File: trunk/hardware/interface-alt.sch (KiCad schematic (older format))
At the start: 19 parts, among them SW1 DIPSW4_DIP, U4 GTL2003

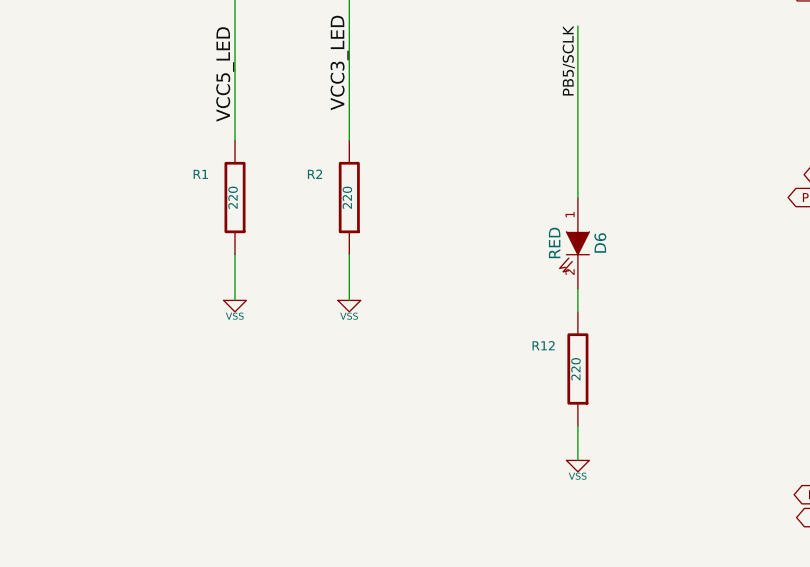
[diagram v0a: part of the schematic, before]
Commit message: Changed all 220ohm LED resistors to 1Kohm. This is how I actually built the first r116 test board. The LEDs are still too bright for my liking, actually. This way, we may also save a little battery power.
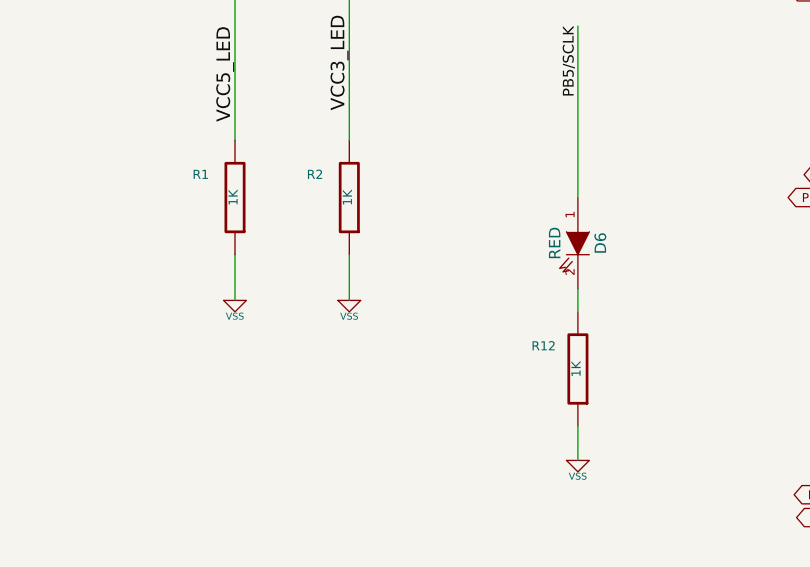
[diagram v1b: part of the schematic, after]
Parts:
- R1, R12, R2: value 220 -> 1K
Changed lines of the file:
@@
 Sheet 6 6
 Title "FREAKDUINO-CHIBI 2.4GHz"
-Date "12 aug 2013"
+Date "13 aug 2013"
 Rev "v1.1"
 Comp "KiCAD version by Gruvin"
@@
 P 6450 5300
 F 0 "R1" H 6600 5200 40  0000 C CNN
-F 1 "220" V 6457 5301 40  0000 C CNN
+F 1 "1K" V 6457 5301 40  0000 C CNN
 F 2 "" V 6380 5300 30  0000 C CNN
 F 3 "" H 6450 5300 30  0000 C CNN
@@
 P 6950 5300
 F 0 "R2" H 7100 5200 40  0000 C CNN
-F 1 "220" V 6957 5301 40  0000 C CNN
+F 1 "1K" V 6957 5301 40  0000 C CNN
 F 2 "" V 6880 5300 30  0000 C CNN
 F 3 "" H 6950 5300 30  0000 C CNN
@@
 P 7950 6050
 F 0 "R12" H 8100 5950 40  0000 C CNN
-F 1 "220" V 7957 6051 40  0000 C CNN
+F 1 "1K" V 7957 6051 40  0000 C CNN
 F 2 "" V 7880 6050 30  0000 C CNN
 F 3 "" H 7950 6050 30  0000 C CNN

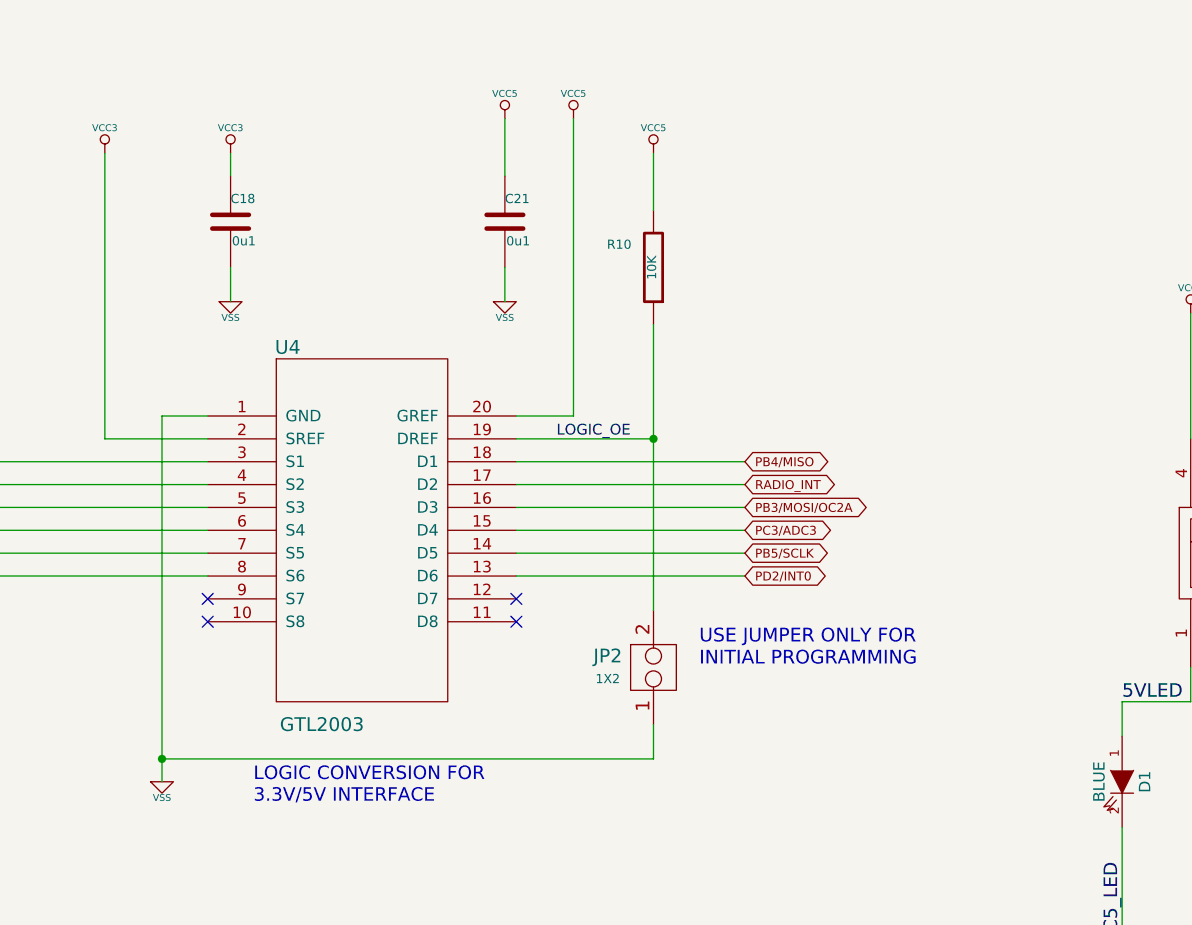
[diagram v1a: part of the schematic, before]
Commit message: Numberous more problems with the circuit design and PCB layout errors found and corrected as a result of debugging and making the RF section work, today, finally.
There remains and issue with the SPI port disable jumper not working as it should -- I think.  I got around this by fluke, when I realised that holding down the reset button (somehow) enables my AVR ISP mkII to program the AVR chip, despite the suspected SPI bus conflict between the ISP and level shofter chip. (Not that any of that makes sense to me right now. But that's what seemed to be the case, at the time. I'll sort it later.)
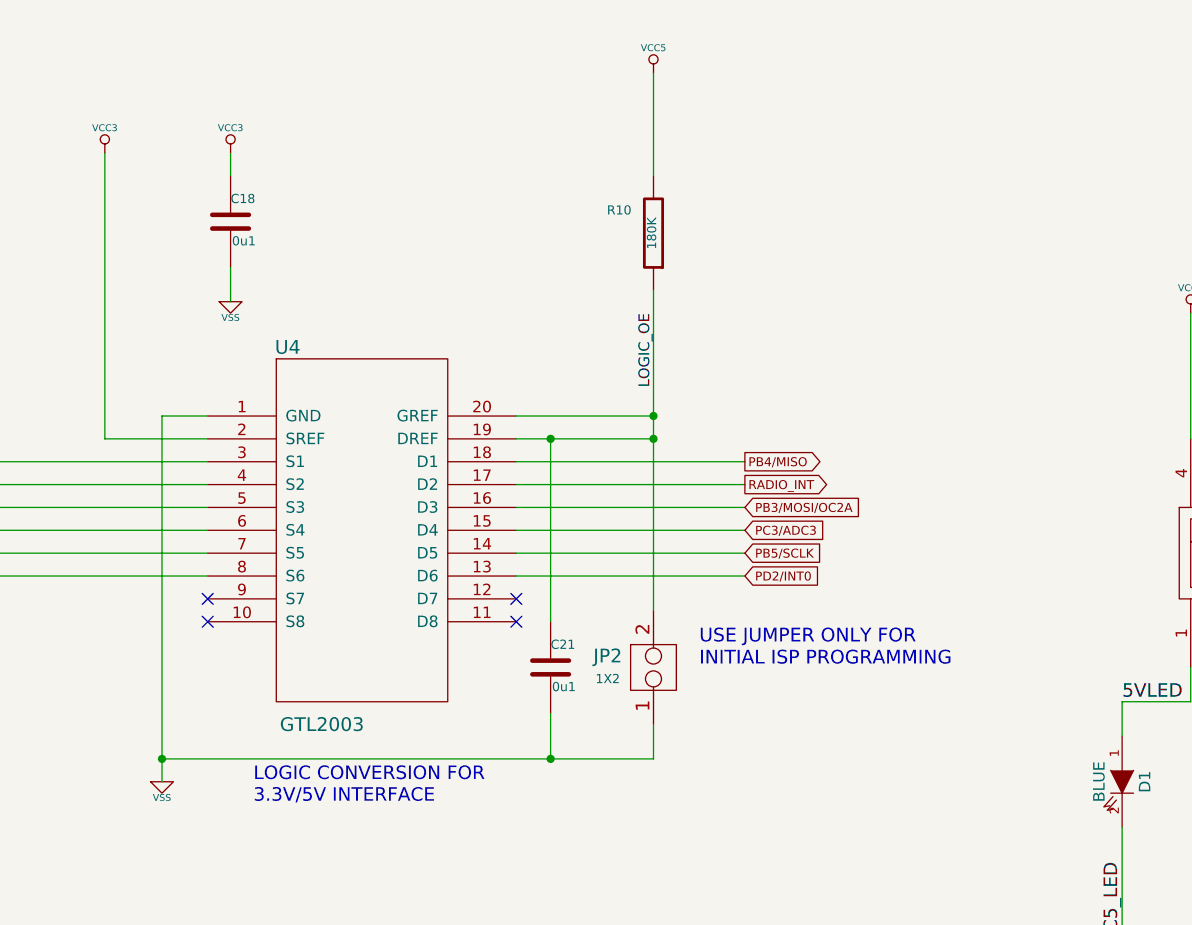
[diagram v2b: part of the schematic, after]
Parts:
- R10: value 10K -> 180K
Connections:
- net LOGIC_OE: now also C21.1, U4.20 (GREF)
- net VCC5: no longer C21.1, U4.20 (GREF)
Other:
- note added: "USE JUMPER ONLY FOR\nINITIAL ISP PROGRAMMING"
- note removed: "USE JUMPER ONLY FOR\nINITIAL PROGRAMMING"
- moved on the sheet: C21, R10
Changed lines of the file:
@@
 Sheet 6 6
 Title "FREAKDUINO-CHIBI 2.4GHz"
-Date "13 aug 2013"
+Date "16 aug 2013"
 Rev "v1.1"
 Comp "KiCAD version by Gruvin"
@@
 L R R10
 U 1 1 51E3DBD0
-P 4400 1950
-F 0 "R10" H 4550 1850 40  0000 C CNN
-F 1 "10K" V 4407 1951 40  0000 C CNN
-F 2 "" V 4330 1950 30  0000 C CNN
-F 3 "" H 4400 1950 30  0000 C CNN
-	1    4400 1950
+P 4400 1800
+F 0 "R10" H 4550 1700 40  0000 C CNN
+F 1 "180K" V 4407 1801 40  0000 C CNN
+F 2 "" V 4330 1800 30  0000 C CNN
+F 3 "" H 4400 1800 30  0000 C CNN
+	1    4400 1800
 	-1   0    0    1
 $EndComp
@@
 L C C21
 U 1 1 51E3DBD6
-P 3750 1750
-F 0 "C21" H 3750 1850 40  0000 L CNN
-F 1 "0u1" H 3756 1665 40  0000 L CNN
-F 2 "" H 3788 1600 30  0000 C CNN
-F 3 "" H 3750 1750 60  0000 C CNN
-	1    3750 1750
-	1    0    0    -1
-$EndComp
-$Comp
-L VSS #PWR051
-U 1 1 51E3DBDC
-P 3750 2100
-F 0 "#PWR051" H 3750 2100 30  0001 C CNN
-F 1 "VSS" H 3750 2030 30  0000 C CNN
-F 2 "" H 3750 2100 60  0000 C CNN
-F 3 "" H 3750 2100 60  0000 C CNN
-	1    3750 2100
-	1    0    0    -1
-$EndComp
-Wire Wire Line
-	3750 1300 3750 1550
-Wire Wire Line
-	3750 1950 3750 2100
+P 3950 3700
+F 0 "C21" H 3950 3800 40  0000 L CNN
+F 1 "0u1" H 3956 3615 40  0000 L CNN
+F 2 "" H 3988 3550 30  0000 C CNN
+F 3 "" H 3950 3700 60  0000 C CNN
+	1    3950 3700
+	1    0    0    -1
+$EndComp
 NoConn ~ 2450 3500
 NoConn ~ 2450 3400
@@
 NoConn ~ 3800 3400
 Wire Wire Line
-	4400 2200 4400 3450
-$Comp
-L VSS #PWR052
+	4400 2050 4400 3450
+$Comp
+L VSS #PWR050
 U 1 1 51E3DBEA
 P 2250 4200
-F 0 "#PWR052" H 2250 4200 30  0001 C CNN
+F 0 "#PWR050" H 2250 4200 30  0001 C CNN
 F 1 "VSS" H 2250 4130 30  0000 C CNN
 F 2 "" H 2250 4200 60  0000 C CNN
@@
 Wire Wire Line
 	2450 3300 1300 3300
-Text Label 4300 2700 2    47   ~ 0
+Text Label 4400 2150 3    47   ~ 0
 LOGIC_OE
 Text GLabel 1300 2800 0    47   Input ~ 0
@@
 SLP_TR
 Wire Wire Line
-	4050 1300 4050 2600
-Wire Wire Line
 	2000 1450 2000 2700
 $Comp
@@
 $EndComp
 $Comp
-L VSS #PWR053
+L VSS #PWR051
 U 1 1 51E3DC0E
 P 2550 2100
-F 0 "#PWR053" H 2550 2100 30  0001 C CNN
+F 0 "#PWR051" H 2550 2100 30  0001 C CNN
 F 1 "VSS" H 2550 2030 30  0000 C CNN
 F 2 "" H 2550 2100 60  0000 C CNN
@@
 	2550 1950 2550 2100
 Wire Wire Line
-	4400 1450 4400 1700
+	4400 1100 4400 1550
 Text Notes 2650 4300 0    59   ~ 0
 LOGIC CONVERSION FOR\n3.3V/5V INTERFACE
@@
 	3800 3300 4800 3300
 $Comp
-L VCC5 #PWR054
-U 1 1 51E3DC24
-P 3750 1300
-F 0 "#PWR054" H 3750 1440 20  0001 C CNN
-F 1 "VCC5" H 3750 1410 30  0000 C CNN
-F 2 "" H 3750 1300 60  0000 C CNN
-F 3 "" H 3750 1300 60  0000 C CNN
-	1    3750 1300
-	1    0    0    -1
-$EndComp
-$Comp
-L VCC5 #PWR055
-U 1 1 51E3DC2A
-P 4050 1300
-F 0 "#PWR055" H 4050 1440 20  0001 C CNN
-F 1 "VCC5" H 4050 1410 30  0000 C CNN
-F 2 "" H 4050 1300 60  0000 C CNN
-F 3 "" H 4050 1300 60  0000 C CNN
-	1    4050 1300
-	1    0    0    -1
-$EndComp
-$Comp
-L VCC3 #PWR056
+L VCC3 #PWR052
 U 1 1 51E3DC30
 P 2000 1450
-F 0 "#PWR056" H 2000 1590 20  0001 C CNN
+F 0 "#PWR052" H 2000 1590 20  0001 C CNN
 F 1 "VCC3" H 2000 1560 30  0000 C CNN
 F 2 "" H 2000 1450 60  0000 C CNN
@@
 $EndComp
 $Comp
-L VCC3 #PWR057
+L VCC3 #PWR053
 U 1 1 51E3DC36
 P 2550 1450
-F 0 "#PWR057" H 2550 1590 20  0001 C CNN
+F 0 "#PWR053" H 2550 1590 20  0001 C CNN
 F 1 "VCC3" H 2550 1560 30  0000 C CNN
 F 2 "" H 2550 1450 60  0000 C CNN
@@
 $EndComp
 Text Notes 4600 3700 0    60   ~ 0
-USE JUMPER ONLY FOR\nINITIAL PROGRAMMING
+USE JUMPER ONLY FOR\nINITIAL ISP PROGRAMMING
 $Comp
 L DIPSW4_DIP SW1
@@
 	6450 4400 6450 5050
 $Comp
-L VSS #PWR058
+L VSS #PWR054
 U 1 1 51E3E179
 P 6450 5750
-F 0 "#PWR058" H 6450 5750 30  0001 C CNN
+F 0 "#PWR054" H 6450 5750 30  0001 C CNN
 F 1 "VSS" H 6450 5680 30  0000 C CNN
 F 2 "" H 6450 5750 60  0000 C CNN
@@
 $EndComp
 $Comp
-L VSS #PWR059
+L VSS #PWR055
 U 1 1 51E3E17F
 P 6950 5750
-F 0 "#PWR059" H 6950 5750 30  0001 C CNN
+F 0 "#PWR055" H 6950 5750 30  0001 C CNN
 F 1 "VSS" H 6950 5680 30  0000 C CNN
 F 2 "" H 6950 5750 60  0000 C CNN
@@
 VCC3_LED
 $Comp
-L VCC3 #PWR060
+L VCC3 #PWR056
 U 1 1 51E3E18C
 P 6950 2350
-F 0 "#PWR060" H 6950 2490 20  0001 C CNN
+F 0 "#PWR056" H 6950 2490 20  0001 C CNN
 F 1 "VCC3" H 6950 2460 30  0000 C CNN
 F 2 "" H 6950 2350 60  0000 C CNN
@@
 $EndComp
 $Comp
-L VCC5 #PWR061
+L VCC5 #PWR057
 U 1 1 51E3E192
 P 6750 2150
-F 0 "#PWR061" H 6750 2290 20  0001 C CNN
+F 0 "#PWR057" H 6750 2290 20  0001 C CNN
 F 1 "VCC5" H 6750 2260 30  0000 C CNN
 F 2 "" H 6750 2150 60  0000 C CNN
@@
 	4200 6300 4200 6600
 $Comp
-L VSS #PWR062
+L VSS #PWR058
 U 1 1 51E3E429
 P 4200 6600
-F 0 "#PWR062" H 4200 6600 30  0001 C CNN
+F 0 "#PWR058" H 4200 6600 30  0001 C CNN
 F 1 "VSS" H 4200 6530 30  0000 C CNN
 F 2 "" H 4200 6600 60  0000 C CNN
@@
 ISP CONNECTOR
 $Comp
-L VCC5 #PWR063
+L VCC5 #PWR059
 U 1 1 51E3E434
 P 4200 5750
-F 0 "#PWR063" H 4200 5890 20  0001 C CNN
+F 0 "#PWR059" H 4200 5890 20  0001 C CNN
 F 1 "VCC5" H 4200 5860 30  0000 C CNN
 F 2 "" H 4200 5750 60  0000 C CNN
@@
 $EndComp
 $Comp
-L VSS #PWR064
+L VSS #PWR060
 U 1 1 51E3E736
 P 7950 6450
-F 0 "#PWR064" H 7950 6450 30  0001 C CNN
+F 0 "#PWR060" H 7950 6450 30  0001 C CNN
 F 1 "VSS" H 7950 6380 30  0000 C CNN
 F 2 "" H 7950 6450 60  0000 C CNN
@@
 	9650 5600 9650 5850
 $Comp
-L VSS #PWR065
+L VSS #PWR061
 U 1 1 51E3E76E
 P 9650 5850
-F 0 "#PWR065" H 9650 5850 30  0001 C CNN
+F 0 "#PWR061" H 9650 5850 30  0001 C CNN
 F 1 "VSS" H 9650 5780 30  0000 C CNN
 F 2 "" H 9650 5850 60  0000 C CNN
@@
 	9100 2100 9100 1000
 $Comp
-L VSS #PWR066
+L VSS #PWR062
 U 1 1 51E3E798
 P 9650 2300
-F 0 "#PWR066" H 9650 2300 30  0001 C CNN
+F 0 "#PWR062" H 9650 2300 30  0001 C CNN
 F 1 "VSS" H 9650 2230 30  0000 C CNN
 F 2 "" H 9650 2300 60  0000 C CNN
@@
 Connection ~ 9650 2000
 $Comp
-L VCC5 #PWR067
+L VCC5 #PWR063
 U 1 1 51E3E7A3
 P 9400 1100
-F 0 "#PWR067" H 9400 1240 20  0001 C CNN
+F 0 "#PWR063" H 9400 1240 20  0001 C CNN
 F 1 "VCC5" H 9400 1210 30  0000 C CNN
 F 2 "" H 9400 1100 60  0000 C CNN
@@
 $EndComp
 $Comp
-L VCC3 #PWR068
+L VCC3 #PWR064
 U 1 1 51E3E7A9
 P 9650 1200
-F 0 "#PWR068" H 9650 1340 20  0001 C CNN
+F 0 "#PWR064" H 9650 1340 20  0001 C CNN
 F 1 "VCC3" H 9650 1310 30  0000 C CNN
 F 2 "" H 9650 1200 60  0000 C CNN
@@
 $EndComp
 $Comp
-L VCC_IN #PWR069
+L VCC_IN #PWR065
 U 1 1 51E3E7C7
 P 9100 1000
-F 0 "#PWR069" H 9100 1140 20  0001 C CNN
+F 0 "#PWR065" H 9100 1140 20  0001 C CNN
 F 1 "VCC_IN" H 9100 1110 30  0000 C CNN
 F 2 "" H 9100 1000 60  0000 C CNN
@@
 Text GLabel 9400 6700 0    39   BiDi ~ 0
 PC5/ADC5/SCL
-Text GLabel 4800 3000 2    39   BiDi ~ 0
+Text GLabel 4800 3000 2    39   Input ~ 0
 PB3/MOSI/OC2A
-Text GLabel 4800 2800 2    39   BiDi ~ 0
+Text GLabel 4800 2800 2    39   Output ~ 0
 PB4/MISO
-Text GLabel 4800 3200 2    39   BiDi ~ 0
+Text GLabel 4800 3200 2    39   Input ~ 0
 PB5/SCLK
-Text GLabel 4800 3300 2    39   BiDi ~ 0
+Text GLabel 4800 3300 2    39   Input ~ 0
 PD2/INT0
-Text GLabel 4800 3100 2    39   BiDi ~ 0
+Text GLabel 4800 3100 2    39   Input ~ 0
 PC3/ADC3
-Text GLabel 4800 2900 2    39   BiDi ~ 0
+Text GLabel 4800 2900 2    39   Output ~ 0
 RADIO_INT
 $Comp
@@
 	2250 2600 2250 4200
 Wire Wire Line
-	4400 3950 4400 4100
-Wire Wire Line
-	4400 4100 2250 4100
+	4400 4100 4400 3950
+Wire Wire Line
+	2250 4100 4400 4100
 Connection ~ 2250 4100
 Wire Wire Line
-	4050 2600 3800 2600
-Wire Wire Line
 	2000 2700 2450 2700
 $Comp
-L VCC5 #PWR070
+L VCC5 #PWR066
 U 1 1 51E5EC37
-P 4400 1450
-F 0 "#PWR070" H 4400 1590 20  0001 C CNN
-F 1 "VCC5" H 4400 1560 30  0000 C CNN
-F 2 "" H 4400 1450 60  0000 C CNN
-F 3 "" H 4400 1450 60  0000 C CNN
-	1    4400 1450
-	1    0    0    -1
-$EndComp
-Wire Wire Line
-	4400 2700 3800 2700
+P 4400 1100
+F 0 "#PWR066" H 4400 1240 20  0001 C CNN
+F 1 "VCC5" H 4400 1210 30  0000 C CNN
+F 2 "" H 4400 1100 60  0000 C CNN
+F 3 "" H 4400 1100 60  0000 C CNN
+	1    4400 1100
+	1    0    0    -1
+$EndComp
+Wire Wire Line
+	3800 2700 4400 2700
 Text GLabel 8650 1600 0    47   Input ~ 0
 RESET_N
+Wire Wire Line
+	3800 2600 4400 2600
+Connection ~ 4400 2600
+Wire Wire Line
+	3950 3500 3950 2700
+Connection ~ 3950 2700
+Wire Wire Line
+	3950 3900 3950 4100
+Connection ~ 3950 4100
 $EndSCHEMATC

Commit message: Final tidy-ups for (hopefully) final PCB fabrication. Bumped version to v1.2.
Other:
- note added: "JUMPER SHOULD NOT BE NEEDED\n(GTL2003 IS OPEN DRAIN OUTPUT)"
- note removed: "USE JUMPER ONLY FOR\nINITIAL ISP PROGRAMMING"
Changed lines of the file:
@@
 Title "FREAKDUINO-CHIBI 2.4GHz"
 Date "16 aug 2013"
-Rev "v1.1"
+Rev "v1.2"
 Comp "KiCAD version by Gruvin"
 Comment1 ""
@@
 U 1 1 51E3DC42
 P 4400 3700
-F 0 "JP2" H 4200 3750 60  0000 C CNN
-F 1 "1X2" H 4200 3650 40  0000 C CNN
+F 0 "JP2" H 4600 3750 60  0000 C CNN
+F 1 "1X2" H 4600 3650 40  0000 C CNN
 F 2 "" H 4400 3700 60  0000 C CNN
 F 3 "" H 4400 3700 60  0000 C CNN
@@
 	1    0    0    -1
 $EndComp
-Text Notes 4600 3700 0    60   ~ 0
-USE JUMPER ONLY FOR\nINITIAL ISP PROGRAMMING
+Text Notes 4500 3950 0    47   ~ 0
+JUMPER SHOULD NOT BE NEEDED\n(GTL2003 IS OPEN DRAIN OUTPUT)
 $Comp
 L DIPSW4_DIP SW1
